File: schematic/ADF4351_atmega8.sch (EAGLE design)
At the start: 85 parts, among them U1 ATMEGA8L-8AU, U2 ADF4351BCPZ, U3 LD1117-3.3V, Y1 25 MHz, Y2 11.0592 MHz

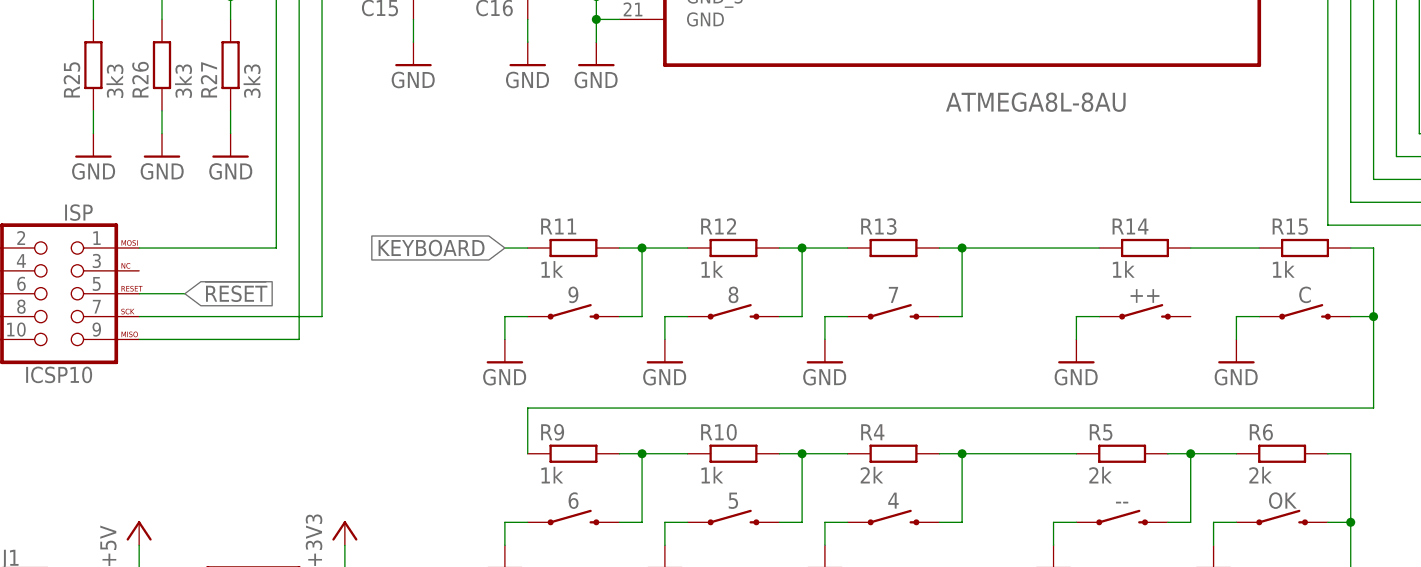
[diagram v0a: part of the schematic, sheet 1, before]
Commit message: Minor fixes in schematic.
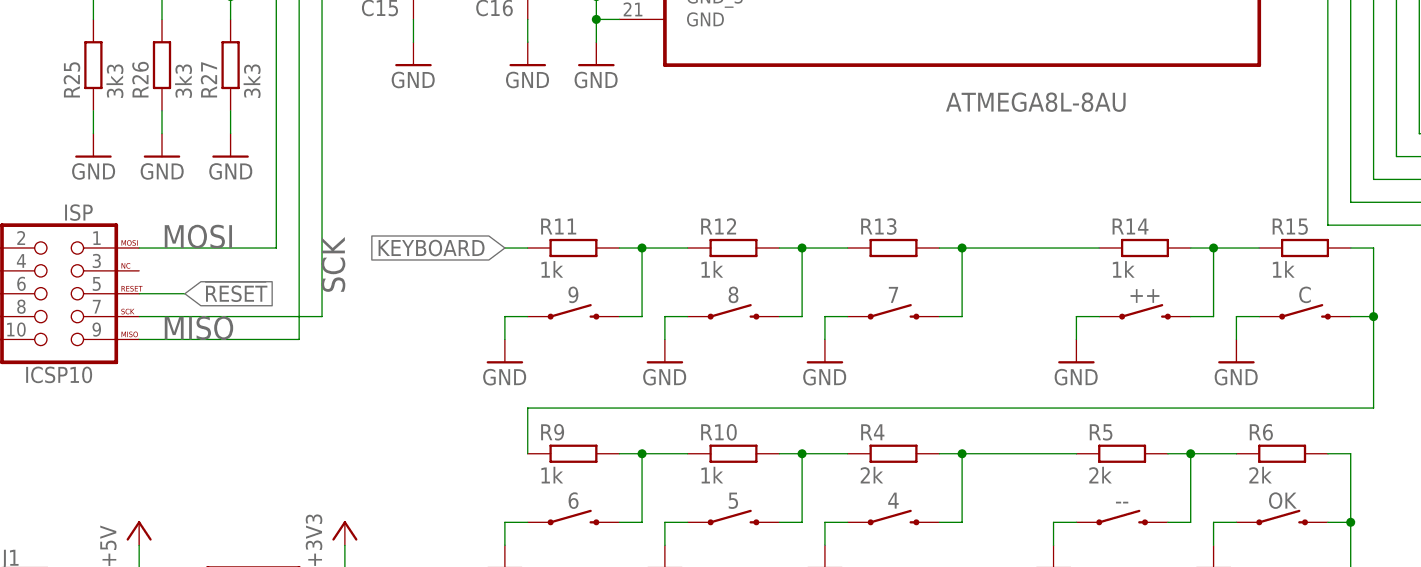
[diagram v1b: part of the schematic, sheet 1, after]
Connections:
- net N$35 renamed SCK
- net N$36 renamed MISO
- net N$37 renamed MOSI
- net N$14: now also ++.2
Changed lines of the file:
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@@
 <pinref part="R14" gate="G$1" pin="2"/>
 <pinref part="R15" gate="G$1" pin="1"/>
-<wire x1="162.56" y1="83.82" x2="170.18" y2="83.82" width="0.1524" layer="91"/>
+<wire x1="162.56" y1="83.82" x2="165.1" y2="83.82" width="0.1524" layer="91"/>
+<pinref part="++" gate="G$1" pin="2"/>
+<wire x1="165.1" y1="83.82" x2="170.18" y2="83.82" width="0.1524" layer="91"/>
+<wire x1="162.56" y1="76.2" x2="165.1" y2="76.2" width="0.1524" layer="91"/>
+<wire x1="165.1" y1="76.2" x2="165.1" y2="83.82" width="0.1524" layer="91"/>
+<junction x="165.1" y="83.82"/>
 </segment>
 </net>
@@
 </segment>
 </net>
-<net name="N$35" class="0">
+<net name="SCK" class="0">
 <segment>
 <pinref part="ISP" gate="G$1" pin="SCK"/>
@@
 <wire x1="66.04" y1="76.2" x2="66.04" y2="124.46" width="0.1524" layer="91"/>
 <wire x1="66.04" y1="124.46" x2="99.06" y2="124.46" width="0.1524" layer="91"/>
-</segment>
-</net>
-<net name="N$36" class="0">
+<label x="68.58" y="78.74" size="2.54" layer="95" rot="R90"/>
+</segment>
+</net>
+<net name="MISO" class="0">
 <segment>
 <pinref part="ISP" gate="G$1" pin="MISO"/>
@@
 <pinref part="U1" gate="A" pin="(MISO)_PB4"/>
 <wire x1="63.5" y1="127" x2="99.06" y2="127" width="0.1524" layer="91"/>
-</segment>
-</net>
-<net name="N$37" class="0">
+<label x="48.26" y="73.66" size="2.54" layer="95"/>
+</segment>
+</net>
+<net name="MOSI" class="0">
 <segment>
 <pinref part="ISP" gate="G$1" pin="MOSI"/>
@@
 <wire x1="60.96" y1="83.82" x2="60.96" y2="129.54" width="0.1524" layer="91"/>
 <wire x1="60.96" y1="129.54" x2="99.06" y2="129.54" width="0.1524" layer="91"/>
+<label x="48.26" y="83.82" size="2.54" layer="95"/>
 </segment>
 </net>
@@
 <pinref part="U2" gate="A" pin="CPOUT"/>
 <wire x1="187.96" y1="137.16" x2="190.5" y2="137.16" width="0.1524" layer="91"/>
-<wire x1="190.5" y1="137.16" x2="190.5" y2="144.78" width="0.1524" layer="91"/>
-<wire x1="190.5" y1="144.78" x2="193.04" y2="144.78" width="0.1524" layer="91"/>
-<label x="193.04" y="144.78" size="1.778" layer="95" xref="yes"/>
-</segment>
-<segment>
+<wire x1="190.5" y1="137.16" x2="190.5" y2="139.7" width="0.1524" layer="91"/>
+<wire x1="190.5" y1="139.7" x2="193.04" y2="139.7" width="0.1524" layer="91"/>
+<label x="193.04" y="139.7" size="1.778" layer="95" xref="yes"/>
+</segment>
+<segment>
